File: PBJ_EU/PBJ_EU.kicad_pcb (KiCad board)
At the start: 2 copper layers, 111.4 x 128.5 mm, 75 parts, among them J1 Molex_47257, J10 Conn_02x05_Odd_Even, J2 Molex_47257, J3 Molex_47257, J4 Molex_47257, J7 Conn_02x05_Odd_Even, J9 Conn_02x08_Odd_Even_Female, SW1 SW_SPDT, SW2 SW_SPDT, SW5 SW_DPST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

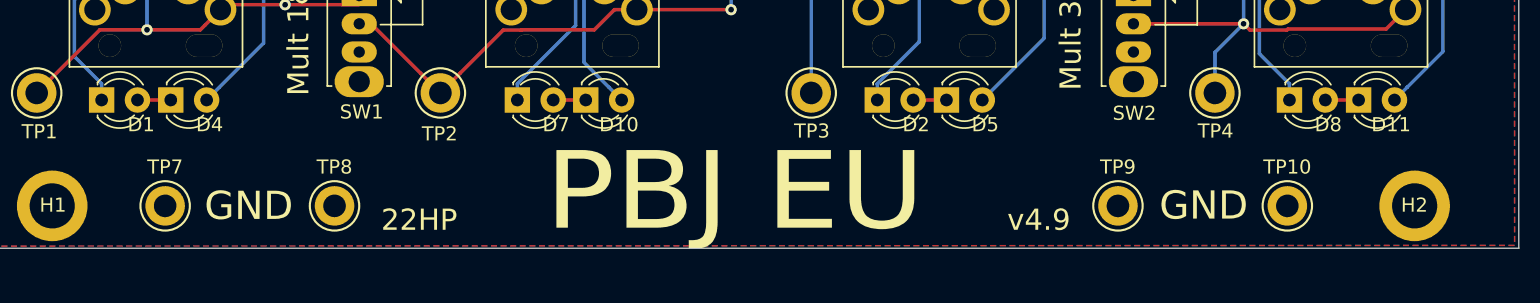
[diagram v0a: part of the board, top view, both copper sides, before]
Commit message: Changed name so that BOM would work
Looks like 6.0 BOM bombs when there is a space in the filename.
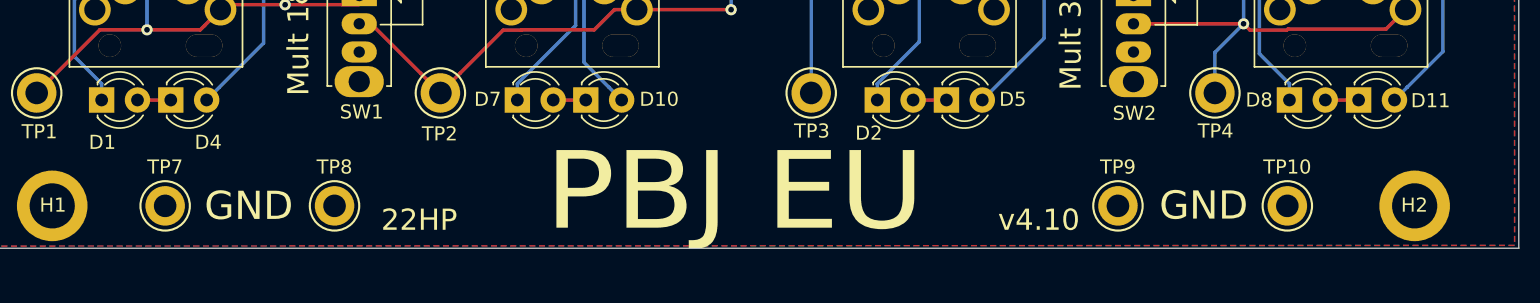
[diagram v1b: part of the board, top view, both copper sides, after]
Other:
- board text added: "v4.10"
- board text removed: "v4.9"
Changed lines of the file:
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@@
   (title_block
     (title "PBJ EU")
-    (rev "4.9")
+    (rev "4.10")
   )
   (layers
@@
   )
   (setup
+    (stackup
+      (layer "F.SilkS" (type "Top Silk Screen"))
+      (layer "F.Paste" (type "Top Solder Paste"))
+      (layer "F.Mask" (type "Top Solder Mask") (thickness 0.01))
+      (layer "F.Cu" (type "copper") (thickness 0.035))
+      (layer "dielectric 1" (type "core") (thickness 1.51) (material "FR4") (epsilon_r 4.5) (loss_tangent 0.02))
+      (layer "B.Cu" (type "copper") (thickness 0.035))
+      (layer "B.Mask" (type "Bottom Solder Mask") (thickness 0.01))
+      (layer "B.Paste" (type "Bottom Solder Paste"))
+      (layer "B.SilkS" (type "Bottom Silk Screen"))
+      (copper_finish "None")
+      (dielectric_constraints no)
+    )
     (pad_to_mask_clearance 0.051)
     (solder_mask_min_width 0.25)
@@
     (property "Sheetname" "")
     (attr through_hole)
-    (fp_text reference "D8" (at 2.75 1.75) (layer "F.SilkS")
+    (fp_text reference "D8" (at -2.15 0) (layer "F.SilkS")
       (effects (font (size 1 1) (thickness 0.15)))
     )
@@
     (property "Sheetname" "")
     (attr through_hole)
-    (fp_text reference "D11" (at 2.3 1.75) (layer "F.SilkS")
+    (fp_text reference "D11" (at 5.1 0.05) (layer "F.SilkS")
       (effects (font (size 1 1) (thickness 0.15)))
     )
@@
     (property "Sheetname" "")
     (attr through_hole)
-    (fp_text reference "D10" (at 2.35 1.75 180) (layer "F.SilkS")
+    (fp_text reference "D10" (at 5.2 -0.05 180) (layer "F.SilkS")
       (effects (font (size 1 1) (thickness 0.15)))
     )
@@
     (property "Sheetname" "")
     (attr through_hole)
-    (fp_text reference "D4" (at 2.75 1.75) (layer "F.SilkS")
+    (fp_text reference "D4" (at 2.65 3) (layer "F.SilkS")
       (effects (font (size 1 1) (thickness 0.15)))
     )
@@
     (property "Sheetname" "")
     (attr through_hole)
-    (fp_text reference "D7" (at 2.75 1.75) (layer "F.SilkS")
+    (fp_text reference "D7" (at -2.1 -0.05) (layer "F.SilkS")
       (effects (font (size 1 1) (thickness 0.15)))
     )
@@
     (property "Sheetname" "")
     (attr through_hole)
-    (fp_text reference "D1" (at 2.8 1.75) (layer "F.SilkS")
+    (fp_text reference "D1" (at 0.05 3) (layer "F.SilkS")
       (effects (font (size 1 1) (thickness 0.15)))
     )
@@
     (property "Sheetname" "")
     (attr through_hole)
-    (fp_text reference "D5" (at 2.75 1.75 180) (layer "F.SilkS")
+    (fp_text reference "D5" (at 4.7 -0.05 180) (layer "F.SilkS")
       (effects (font (size 1 1) (thickness 0.15)))
     )
@@
     (property "Sheetname" "")
     (attr through_hole)
-    (fp_text reference "D2" (at 2.75 1.75) (layer "F.SilkS")
+    (fp_text reference "D2" (at -0.6 2.35) (layer "F.SilkS")
       (effects (font (size 1 1) (thickness 0.15)))
     )
@@
     (effects (font (size 2 2) (thickness 0.4)))
   )
-  (gr_text "v4.9" (at 117.4 156.5) (layer "F.SilkS")
+  (gr_text "v4.10" (at 117.4 156.5) (layer "F.SilkS")
     (effects (font (size 1.5 1.5) (thickness 0.2)))
   )
